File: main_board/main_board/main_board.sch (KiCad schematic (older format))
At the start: 12 parts, among them J1 jstsh4x1, J2 jstsh4x1, J3 jstsh8x1, J4 jstsh8x1, J5 jstsh8x1, J6 jstsh8x1, J7 jstsh2x1, U1 Teensy3.5_All_Pins

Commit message: added more to the mainboard/daugher board
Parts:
- removed J1, J2: jstsh4x1, exocam_charge_amp:jstsh4x1, symbol exocam_charge_amp:jstsh4x1
- removed J3, J4, J5, J6: jstsh8x1, exocam_charge_amp:jstsh8x1, symbol exocam_charge_amp:jstsh8x1
- removed J7: jstsh2x1, exocam_charge_amp:jstsh2x1, symbol exocam_charge_amp:jstsh2x1
- added J1, J2: jstsh5x1, symbol exocam_charge_amp:jstsh5x1
- added J3, J4, J5, J6: jstsh9x1, symbol exocam_charge_amp:jstsh9x1
- added J7: jstsh4x1, symbol exocam_charge_amp:jstsh4x1
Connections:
- net labels added: VBat
- wire segments 70 -> 71
- no-connect marks 0 -> 15
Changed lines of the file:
@@
-$EndComp
-$Comp
-L exocam_charge_amp:jstsh4x1 J1
-U 1 1 60F03F4F
-P 5050 1100
-F 0 "J1" V 4850 900 50  0000 L CNN
-F 1 "jstsh4x1" V 4750 750 50  0000 L CNN
-F 2 "exocam_charge_amp:jstsh4x1" H 5000 1250 50  0001 C CNN
-F 3 "" H 5000 1250 50  0001 C CNN
-	1    5050 1100
-	0    -1   -1   0
-$EndComp
-$Comp
-L exocam_charge_amp:jstsh4x1 J2
-U 1 1 60F04A69
-P 6150 1000
-F 0 "J2" V 5950 800 50  0000 L CNN
-F 1 "jstsh4x1" V 5850 650 50  0000 L CNN
-F 2 "exocam_charge_amp:jstsh4x1" H 6100 1150 50  0001 C CNN
-F 3 "" H 6100 1150 50  0001 C CNN
-	1    6150 1000
-	0    -1   -1   0
-$EndComp
-$Comp
-L exocam_charge_amp:jstsh8x1 J3
-U 1 1 60F07789
-P 6850 1000
-F 0 "J3" V 6667 547 50  0000 C CNN
-F 1 "jstsh8x1" V 6576 547 50  0000 C CNN
-F 2 "exocam_charge_amp:jstsh8x1" H 6800 1150 50  0001 C CNN
-F 3 "" H 6800 1150 50  0001 C CNN
-	1    6850 1000
-	0    -1   -1   0
-$EndComp
-$Comp
-L exocam_charge_amp:jstsh8x1 J4
-U 1 1 60F08417
-P 8150 1000
-F 0 "J4" V 7967 547 50  0000 C CNN
-F 1 "jstsh8x1" V 7876 547 50  0000 C CNN
-F 2 "exocam_charge_amp:jstsh8x1" H 8100 1150 50  0001 C CNN
-F 3 "" H 8100 1150 50  0001 C CNN
-	1    8150 1000
-	0    -1   -1   0
 $EndComp
 $Comp
@@
 L power:GND #PWR0107
 U 1 1 60F10D73
-P 8000 800
-F 0 "#PWR0107" H 8000 550 50  0001 C CNN
-F 1 "GND" H 8005 627 50  0000 C CNN
-F 2 "" H 8000 800 50  0001 C CNN
-F 3 "" H 8000 800 50  0001 C CNN
-	1    8000 800
-	1    0    0    -1
-$EndComp
-Wire Wire Line
-	8000 800  8200 800
-Wire Wire Line
-	8200 800  8200 900
+P 7900 750
+F 0 "#PWR0107" H 7900 500 50  0001 C CNN
+F 1 "GND" H 7905 577 50  0000 C CNN
+F 2 "" H 7900 750 50  0001 C CNN
+F 3 "" H 7900 750 50  0001 C CNN
+	1    7900 750
+	1    0    0    -1
+$EndComp
 $Comp
 L exocam_charge_amp-cache:+3.3V #PWR0108
 U 1 1 60F118AC
-P 8900 750
-F 0 "#PWR0108" H 8900 600 50  0001 C CNN
-F 1 "+3.3V" H 9000 900 50  0000 C CNN
-F 2 "" H 8900 750 50  0001 C CNN
-F 3 "" H 8900 750 50  0001 C CNN
-	1    8900 750
-	1    0    0    -1
-$EndComp
-Wire Wire Line
-	8900 900  8900 750
+P 8800 750
+F 0 "#PWR0108" H 8800 600 50  0001 C CNN
+F 1 "+3.3V" H 8900 900 50  0000 C CNN
+F 2 "" H 8800 750 50  0001 C CNN
+F 3 "" H 8800 750 50  0001 C CNN
+	1    8800 750
+	1    0    0    -1
+$EndComp
+Wire Wire Line
+	8800 900  8800 750
 Wire Wire Line
 	5200 1000 5200 900
@@
 Wire Wire Line
 	7500 850  7500 900
+Text GLabel 8200 850  1    50   Input ~ 0
+AMP6
 Text GLabel 8300 850  1    50   Input ~ 0
-AMP6
+UNAMP6
 Text GLabel 8400 850  1    50   Input ~ 0
-UNAMP6
+AMP7
+Text GLabel 8700 850  1    50   Input ~ 0
+UNAMP8
 Text GLabel 8500 850  1    50   Input ~ 0
-AMP7
-Text GLabel 8800 850  1    50   Input ~ 0
-UNAMP8
+UNAMP7
 Text GLabel 8600 850  1    50   Input ~ 0
-UNAMP7
-Text GLabel 8700 850  1    50   Input ~ 0
 AMP8
 Wire Wire Line
+	8200 850  8200 900
+Wire Wire Line
 	8300 850  8300 900
 Wire Wire Line
@@
 Wire Wire Line
 	8700 850  8700 900
-Wire Wire Line
-	8800 850  8800 900
-$Comp
-L exocam_charge_amp:jstsh8x1 J5
-U 1 1 60F28CDD
-P 6850 1950
-F 0 "J5" V 6667 1497 50  0000 C CNN
-F 1 "jstsh8x1" V 6576 1497 50  0000 C CNN
-F 2 "exocam_charge_amp:jstsh8x1" H 6800 2100 50  0001 C CNN
-F 3 "" H 6800 2100 50  0001 C CNN
-	1    6850 1950
-	0    -1   -1   0
-$EndComp
 $Comp
 L power:GND #PWR0109
@@
 	7500 1800 7500 1850
 $Comp
-L exocam_charge_amp:jstsh8x1 J6
-U 1 1 60F2BB41
-P 8100 1950
-F 0 "J6" V 7917 1497 50  0000 C CNN
-F 1 "jstsh8x1" V 7826 1497 50  0000 C CNN
-F 2 "exocam_charge_amp:jstsh8x1" H 8050 2100 50  0001 C CNN
-F 3 "" H 8050 2100 50  0001 C CNN
-	1    8100 1950
-	0    -1   -1   0
-$EndComp
-$Comp
 L power:GND #PWR0111
 U 1 1 60F2BB47
@@
 	1400 4700 1450 4700
 $Comp
-L exocam_charge_amp:jstsh2x1 J7
-U 1 1 60FD52E4
-P 4300 1050
-F 0 "J7" V 4150 900 50  0000 L CNN
-F 1 "jstsh2x1" V 4000 800 50  0000 L CNN
-F 2 "exocam_charge_amp:jstsh2x1" H 4250 1200 50  0001 C CNN
-F 3 "" H 4250 1200 50  0001 C CNN
-	1    4300 1050
-	0    -1   -1   0
-$EndComp
-$Comp
-L power:GND #PWR0115
-U 1 1 60FD96AC
-P 4100 800
-F 0 "#PWR0115" H 4100 550 50  0001 C CNN
-F 1 "GND" H 4105 627 50  0000 C CNN
-F 2 "" H 4100 800 50  0001 C CNN
-F 3 "" H 4100 800 50  0001 C CNN
-	1    4100 800
-	1    0    0    -1
-$EndComp
-Wire Wire Line
-	4350 950  4350 800
-Wire Wire Line
-	4350 800  4100 800
-$Comp
-L exocam_charge_amp-cache:+3.3V #PWR0116
-U 1 1 60FDB60B
-P 4450 800
-F 0 "#PWR0116" H 4450 650 50  0001 C CNN
-F 1 "+3.3V" H 4465 973 50  0000 C CNN
-F 2 "" H 4450 800 50  0001 C CNN
-F 3 "" H 4450 800 50  0001 C CNN
-	1    4450 800
-	1    0    0    -1
-$EndComp
-Wire Wire Line
-	4450 950  4450 800
+L exocam_charge_amp:jstsh4x1 J7
+U 1 1 6111A17F
+P 4100 1100
+F 0 "J7" V 4149 1138 50  0000 L CNN
+F 1 "jstsh4x1" V 4058 1138 50  0000 L CNN
+F 2 "" H 4050 1250 50  0001 C CNN
+F 3 "" H 4050 1250 50  0001 C CNN
+	1    4100 1100
+	0    -1   -1   0
+$EndComp
+Text GLabel 4250 850  1    50   Input ~ 0
+VBat
+Wire Wire Line
+	4250 850  4250 1000
+Wire Wire Line
+	4150 1000 4150 850
+Wire Wire Line
+	4150 850  4050 850
+$Comp
+L power:GND #PWR?
+U 1 1 61120BE1
+P 4050 850
+F 0 "#PWR?" H 4050 600 50  0001 C CNN
+F 1 "GND" H 3900 750 50  0000 C CNN
+F 2 "" H 4050 850 50  0001 C CNN
+F 3 "" H 4050 850 50  0001 C CNN
+	1    4050 850
+	1    0    0    -1
+$EndComp
+NoConn ~ 4350 1000
+NoConn ~ 4450 1000
+NoConn ~ 4600 1150
+$Comp
+L exocam_charge_amp:jstsh9x1 J4
+U 1 1 611383AD
+P 8050 1000
+F 0 "J4" V 7867 497 50  0000 C CNN
+F 1 "jstsh9x1" V 7776 497 50  0000 C CNN
+F 2 "" H 8000 1150 50  0001 C CNN
+F 3 "" H 8000 1150 50  0001 C CNN
+	1    8050 1000
+	0    -1   -1   0
+$EndComp
+NoConn ~ 8900 900
+NoConn ~ 9050 1050
+$Comp
+L exocam_charge_amp:jstsh9x1 J6
+U 1 1 61149A31
+P 8100 1950
+F 0 "J6" V 7917 1447 50  0000 C CNN
+F 1 "jstsh9x1" V 7826 1447 50  0000 C CNN
+F 2 "" H 8050 2100 50  0001 C CNN
+F 3 "" H 8050 2100 50  0001 C CNN
+	1    8100 1950
+	0    -1   -1   0
+$EndComp
+NoConn ~ 8950 1850
+NoConn ~ 9100 2000
+$Comp
+L exocam_charge_amp:jstsh9x1 J5
+U 1 1 6114F267
+P 6850 1950
+F 0 "J5" V 6667 1447 50  0000 C CNN
+F 1 "jstsh9x1" V 6576 1447 50  0000 C CNN
+F 2 "" H 6800 2100 50  0001 C CNN
+F 3 "" H 6800 2100 50  0001 C CNN
+	1    6850 1950
+	0    -1   -1   0
+$EndComp
+NoConn ~ 7700 1850
+NoConn ~ 7850 2000
+$Comp
+L exocam_charge_amp:jstsh9x1 J3
+U 1 1 61153EFD
+P 6850 1000
+F 0 "J3" V 6667 497 50  0000 C CNN
+F 1 "jstsh9x1" V 6576 497 50  0000 C CNN
+F 2 "" H 6800 1150 50  0001 C CNN
+F 3 "" H 6800 1150 50  0001 C CNN
+	1    6850 1000
+	0    -1   -1   0
+$EndComp
+Wire Wire Line
+	8100 750  7900 750
+Wire Wire Line
+	8100 750  8100 900
+NoConn ~ 7700 900
+NoConn ~ 7850 1050
+Text GLabel 4200 5100 2    50   Input ~ 0
+VBat
+Wire Wire Line
+	4200 5100 3750 5100
+$Comp
+L exocam_charge_amp:jstsh5x1 J1
+U 1 1 61179B31
+P 5050 1100
+F 0 "J1" V 5074 1138 50  0000 L CNN
+F 1 "jstsh5x1" V 4983 1138 50  0000 L CNN
+F 2 "" H 5000 1250 50  0001 C CNN
+F 3 "" H 5000 1250 50  0001 C CNN
+	1    5050 1100
+	0    -1   -1   0
+$EndComp
+$Comp
+L exocam_charge_amp:jstsh5x1 J2
+U 1 1 6117E179
+P 6150 1000
+F 0 "J2" V 6174 1038 50  0000 L CNN
+F 1 "jstsh5x1" V 6083 1038 50  0000 L CNN
+F 2 "" H 6100 1150 50  0001 C CNN
+F 3 "" H 6100 1150 50  0001 C CNN
+	1    6150 1000
+	0    -1   -1   0
+$EndComp
+NoConn ~ 6700 1100
+NoConn ~ 6600 900
+NoConn ~ 5500 1000
+NoConn ~ 5600 1200
 $EndSCHEMATC

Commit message: updated changes pertaining to daughter board
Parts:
- J1, J2: footprint (none) -> exocam_charge_amp:jstsh5x1
- J3, J4, J5, J6: footprint (none) -> exocam_charge_amp:jstsh9x1
- J7: footprint (none) -> exocam_charge_amp:jstsh4x1
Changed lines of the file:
@@
 F 0 "J7" V 4149 1138 50  0000 L CNN
 F 1 "jstsh4x1" V 4058 1138 50  0000 L CNN
-F 2 "" H 4050 1250 50  0001 C CNN
+F 2 "exocam_charge_amp:jstsh4x1" H 4050 1250 50  0001 C CNN
 F 3 "" H 4050 1250 50  0001 C CNN
 	1    4100 1100
@@
 	4150 850  4050 850
 $Comp
-L power:GND #PWR?
+L power:GND #PWR0115
 U 1 1 61120BE1
 P 4050 850
-F 0 "#PWR?" H 4050 600 50  0001 C CNN
+F 0 "#PWR0115" H 4050 600 50  0001 C CNN
 F 1 "GND" H 3900 750 50  0000 C CNN
 F 2 "" H 4050 850 50  0001 C CNN
@@
 F 0 "J4" V 7867 497 50  0000 C CNN
 F 1 "jstsh9x1" V 7776 497 50  0000 C CNN
-F 2 "" H 8000 1150 50  0001 C CNN
+F 2 "exocam_charge_amp:jstsh9x1" H 8000 1150 50  0001 C CNN
 F 3 "" H 8000 1150 50  0001 C CNN
 	1    8050 1000
@@
 F 0 "J6" V 7917 1447 50  0000 C CNN
 F 1 "jstsh9x1" V 7826 1447 50  0000 C CNN
-F 2 "" H 8050 2100 50  0001 C CNN
+F 2 "exocam_charge_amp:jstsh9x1" H 8050 2100 50  0001 C CNN
 F 3 "" H 8050 2100 50  0001 C CNN
 	1    8100 1950
@@
 F 0 "J5" V 6667 1447 50  0000 C CNN
 F 1 "jstsh9x1" V 6576 1447 50  0000 C CNN
-F 2 "" H 6800 2100 50  0001 C CNN
+F 2 "exocam_charge_amp:jstsh9x1" H 6800 2100 50  0001 C CNN
 F 3 "" H 6800 2100 50  0001 C CNN
 	1    6850 1950
@@
 F 0 "J3" V 6667 497 50  0000 C CNN
 F 1 "jstsh9x1" V 6576 497 50  0000 C CNN
-F 2 "" H 6800 1150 50  0001 C CNN
+F 2 "exocam_charge_amp:jstsh9x1" H 6800 1150 50  0001 C CNN
 F 3 "" H 6800 1150 50  0001 C CNN
 	1    6850 1000
@@
 F 0 "J1" V 5074 1138 50  0000 L CNN
 F 1 "jstsh5x1" V 4983 1138 50  0000 L CNN
-F 2 "" H 5000 1250 50  0001 C CNN
+F 2 "exocam_charge_amp:jstsh5x1" H 5000 1250 50  0001 C CNN
 F 3 "" H 5000 1250 50  0001 C CNN
 	1    5050 1100
@@
 F 0 "J2" V 6174 1038 50  0000 L CNN
 F 1 "jstsh5x1" V 6083 1038 50  0000 L CNN
-F 2 "" H 6100 1150 50  0001 C CNN
+F 2 "exocam_charge_amp:jstsh5x1" H 6100 1150 50  0001 C CNN
 F 3 "" H 6100 1150 50  0001 C CNN
 	1    6150 1000

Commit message: some more layouting of the daugher board
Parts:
- removed J1, J2: jstsh5x1, exocam_charge_amp:jstsh5x1, symbol exocam_charge_amp:jstsh5x1
- removed J3, J4, J5, J6: jstsh9x1, exocam_charge_amp:jstsh9x1, symbol exocam_charge_amp:jstsh9x1
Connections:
- net labels removed: UNAMP1, UNAMP10, UNAMP11, UNAMP12, UNAMP13, UNAMP14, UNAMP2, UNAMP3, UNAMP4, UNAMP5, UNAMP6, UNAMP7, UNAMP8, UNAMP9
- wire segments 71 -> 23
- no-connect marks 15 -> 3

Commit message: more layout changes for daughter board
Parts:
- renumbered J7 to J1
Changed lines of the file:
@@
 	1400 4700 1450 4700
 $Comp
-L exocam_charge_amp:jstsh4x1 J7
+L exocam_charge_amp:jstsh4x1 J1
 U 1 1 6111A17F
 P 4100 1100
-F 0 "J7" V 4149 1138 50  0000 L CNN
+F 0 "J1" V 4149 1138 50  0000 L CNN
 F 1 "jstsh4x1" V 4058 1138 50  0000 L CNN
 F 2 "exocam_charge_amp:jstsh4x1" H 4050 1250 50  0001 C CNN

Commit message: first version of daughter board with pinout
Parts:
- added H5: MountingHole-Mechanical, exocam_charge_amp:mount_hole_2.5mm, symbol exocam_charge_amp-rescue:MountingHole-Mechanical
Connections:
- net GND: now also U1.27 (GND), U1.39 (GND), U1.61 (GND), U1.62 (GND)
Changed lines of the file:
@@
 Wire Wire Line
 	4200 5100 3750 5100
+$Comp
+L exocam_charge_amp-rescue:MountingHole-Mechanical H5
+U 1 1 61037EA1
+P 6800 3600
+F 0 "H5" H 6900 3646 50  0000 L CNN
+F 1 "MountingHole-Mechanical" H 6900 3555 50  0000 L CNN
+F 2 "exocam_charge_amp:mount_hole_2.5mm" H 6800 3600 50  0001 C CNN
+F 3 "" H 6800 3600 50  0001 C CNN
+	1    6800 3600
+	1    0    0    -1
+$EndComp
+$Comp
+L power:GND #PWR?
+U 1 1 61051878
+P 3900 4000
+F 0 "#PWR?" H 3900 3750 50  0001 C CNN
+F 1 "GND" H 3905 3827 50  0000 C CNN
+F 2 "" H 3900 4000 50  0001 C CNN
+F 3 "" H 3900 4000 50  0001 C CNN
+	1    3900 4000
+	1    0    0    -1
+$EndComp
+Wire Wire Line
+	3750 4000 3900 4000
+Wire Wire Line
+	3750 4100 3750 4000
+Connection ~ 3750 4000
+$Comp
+L power:GND #PWR?
+U 1 1 6105371B
+P 1050 5400
+F 0 "#PWR?" H 1050 5150 50  0001 C CNN
+F 1 "GND" H 1055 5227 50  0000 C CNN
+F 2 "" H 1050 5400 50  0001 C CNN
+F 3 "" H 1050 5400 50  0001 C CNN
+	1    1050 5400
+	1    0    0    -1
+$EndComp
+Wire Wire Line
+	1450 5400 1050 5400
+$Comp
+L power:GND #PWR?
+U 1 1 610550ED
+P 1050 4200
+F 0 "#PWR?" H 1050 3950 50  0001 C CNN
+F 1 "GND" H 1055 4027 50  0000 C CNN
+F 2 "" H 1050 4200 50  0001 C CNN
+F 3 "" H 1050 4200 50  0001 C CNN
+	1    1050 4200
+	1    0    0    -1
+$EndComp
+Wire Wire Line
+	1450 4200 1050 4200
 $EndSCHEMATC

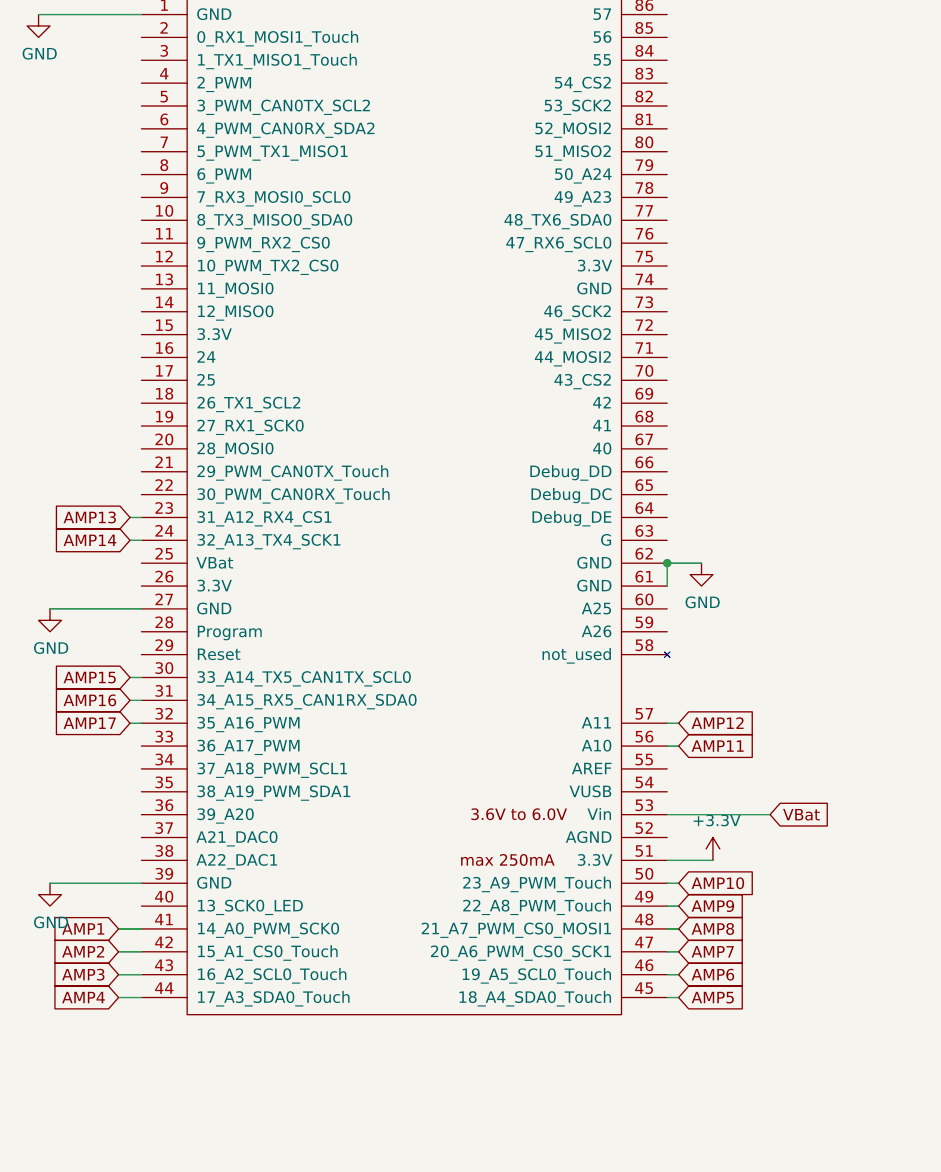
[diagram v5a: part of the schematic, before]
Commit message: redid daughter board as the time frame and cost was too much with 4 layers (an not really needed).
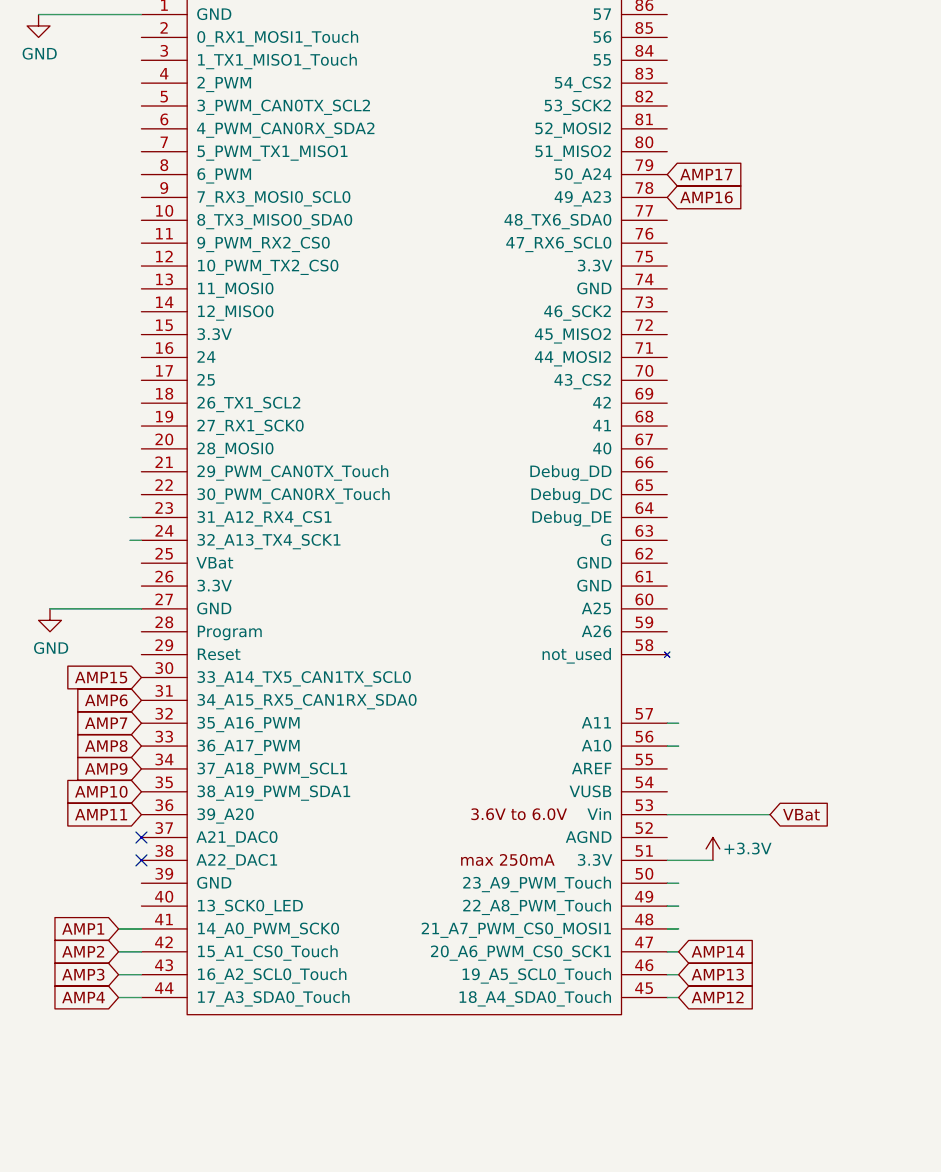
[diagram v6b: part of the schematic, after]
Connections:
- net labels removed: AMP5
- wire segments 27 -> 21
- no-connect marks 3 -> 5
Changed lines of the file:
@@
 P 3950 5300
 F 0 "#PWR0113" H 3950 5150 50  0001 C CNN
-F 1 "+3.3V" H 3965 5473 50  0000 C CNN
+F 1 "+3.3V" H 4100 5350 50  0000 C CNN
 F 2 "" H 3950 5300 50  0001 C CNN
 F 3 "" H 3950 5300 50  0001 C CNN
@@
 Wire Wire Line
 	1350 5900 1450 5900
-Text GLabel 3800 5900 2    50   Input ~ 0
-AMP5
 Wire Wire Line
 	3750 5900 3800 5900
-Text GLabel 3800 5800 2    50   Input ~ 0
-AMP6
 Wire Wire Line
 	3750 5800 3800 5800
-Text GLabel 3800 5700 2    50   Input ~ 0
-AMP7
 Wire Wire Line
 	3750 5700 3800 5700
-Text GLabel 3800 5600 2    50   Input ~ 0
-AMP8
 Wire Wire Line
 	3750 5600 3800 5600
-Text GLabel 3800 5500 2    50   Input ~ 0
-AMP9
 Wire Wire Line
 	3750 5500 3800 5500
-Text GLabel 3800 5400 2    50   Input ~ 0
-AMP10
 Wire Wire Line
 	3750 5400 3800 5400
-Text GLabel 3800 4800 2    50   Input ~ 0
+Text GLabel 1450 5100 0    50   Input ~ 0
 AMP11
 Wire Wire Line
 	3750 4800 3800 4800
-Text GLabel 3800 4700 2    50   Input ~ 0
+Text GLabel 3800 5900 2    50   Input ~ 0
 AMP12
 Wire Wire Line
 	3750 4700 3800 4700
-Text GLabel 1400 3800 0    50   Input ~ 0
+Text GLabel 3800 5800 2    50   Input ~ 0
 AMP13
 Wire Wire Line
 	1400 3800 1450 3800
-Text GLabel 1400 3900 0    50   Input ~ 0
+Text GLabel 3800 5700 2    50   Input ~ 0
 AMP14
 Wire Wire Line
 	1400 3900 1450 3900
-Text GLabel 1400 4500 0    50   Input ~ 0
-AMP15
-Wire Wire Line
-	1400 4500 1450 4500
-Text GLabel 1400 4600 0    50   Input ~ 0
-AMP16
-Wire Wire Line
-	1400 4600 1450 4600
-Text GLabel 1400 4700 0    50   Input ~ 0
-AMP17
-Wire Wire Line
-	1400 4700 1450 4700
 $Comp
 L exocam_charge_amp:jstsh4x1 J1
@@
 $EndComp
 $Comp
-L power:GND #PWR?
-U 1 1 61051878
-P 3900 4000
-F 0 "#PWR?" H 3900 3750 50  0001 C CNN
-F 1 "GND" H 3905 3827 50  0000 C CNN
-F 2 "" H 3900 4000 50  0001 C CNN
-F 3 "" H 3900 4000 50  0001 C CNN
-	1    3900 4000
-	1    0    0    -1
-$EndComp
-Wire Wire Line
-	3750 4000 3900 4000
-Wire Wire Line
-	3750 4100 3750 4000
-Connection ~ 3750 4000
-$Comp
-L power:GND #PWR?
-U 1 1 6105371B
-P 1050 5400
-F 0 "#PWR?" H 1050 5150 50  0001 C CNN
-F 1 "GND" H 1055 5227 50  0000 C CNN
-F 2 "" H 1050 5400 50  0001 C CNN
-F 3 "" H 1050 5400 50  0001 C CNN
-	1    1050 5400
-	1    0    0    -1
-$EndComp
-Wire Wire Line
-	1450 5400 1050 5400
-$Comp
-L power:GND #PWR?
+L power:GND #PWR0103
 U 1 1 610550ED
 P 1050 4200
-F 0 "#PWR?" H 1050 3950 50  0001 C CNN
+F 0 "#PWR0103" H 1050 3950 50  0001 C CNN
 F 1 "GND" H 1055 4027 50  0000 C CNN
 F 2 "" H 1050 4200 50  0001 C CNN
@@
 Wire Wire Line
 	1450 4200 1050 4200
+Text GLabel 3750 2300 2    50   Input ~ 0
+AMP17
+NoConn ~ 1450 5200
+NoConn ~ 1450 5300
+Text GLabel 1450 4600 0    50   Input ~ 0
+AMP6
+Text GLabel 1450 4700 0    50   Input ~ 0
+AMP7
+Text GLabel 1450 4800 0    50   Input ~ 0
+AMP8
+Text GLabel 1450 4900 0    50   Input ~ 0
+AMP9
+Text GLabel 1450 5000 0    50   Input ~ 0
+AMP10
+Text GLabel 3750 2400 2    50   Input ~ 0
+AMP16
+Text GLabel 1450 4500 0    50   Input ~ 0
+AMP15
 $EndSCHEMATC
